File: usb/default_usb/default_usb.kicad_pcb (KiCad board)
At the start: 2 copper layers, 4 parts

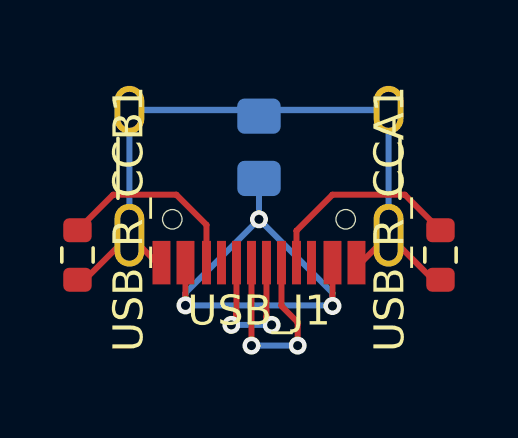
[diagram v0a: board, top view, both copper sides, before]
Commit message: updat e-paper module
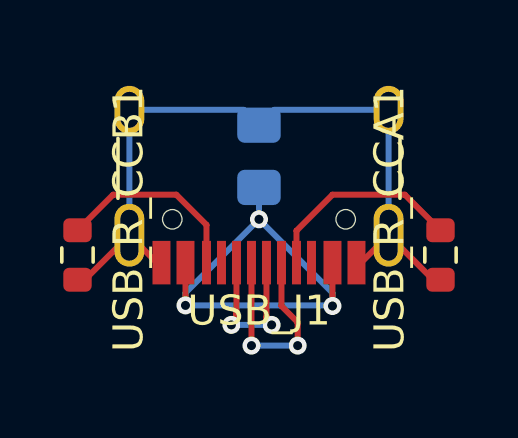
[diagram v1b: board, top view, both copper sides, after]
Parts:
- moved USB_C1 0.30 mm to (0.00, 0.50)
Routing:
- net GND: track 33.9 -> 25.5 mm
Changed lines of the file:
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@@
 		(fp_line
 			(start 5.32 -5.27)
-			(end 5.32 2.6)
-			(stroke
-				(width 0.05)
-				(type solid)
-			)
-			(layer "F.CrtYd")
-		)
-		(fp_line
-			(start -5.32 2.6)
-			(end 5.32 2.6)
+			(end 5.32 2.4)
+			(stroke
+				(width 0.05)
+				(type solid)
+			)
+			(layer "F.CrtYd")
+		)
+		(fp_line
+			(start -5.32 2.4)
+			(end 5.32 2.4)
 			(stroke
 				(width 0.05)
@@
 		(fp_line
 			(start -5.32 -5.27)
-			(end -5.32 2.6)
+			(end -5.32 2.4)
 			(stroke
 				(width 0.05)
@@
 		)
 		(embedded_fonts no)
-		(model "/Users/jinsongc/Development/ErgoCaiLib/3dmodels/TYPE-C-31-M-12--3DModel-STEP-56544.STEP"
+		(model "${KICAD8_3RD_PARTY}/3dmodels/com_github_ebastler_marbastlib/CON_TYPE-C-31-M-12.step"
 			(offset
-				(xyz 0 -1 0.04)
+				(xyz -4.47 -3.65 0.04)
 			)
 			(scale
@@
 			)
 			(rotate
-				(xyz 90 180 -180)
+				(xyz 0 0 0)
 			)
 		)
@@
 	(footprint "ErgoCai.pretty:C_0805_2012Metric_Pad1.18x1.45mm_HandSolder"
 		(layer "B.Cu")
-		(at 0 0.2 -90)
+		(at 0 0.5 -90)
 		(descr "Capacitor SMD 0805 (2012 Metric), square (rectangular) end terminal, IPC_7351 nominal with elongated pad for handsoldering. (Body size source: IPC-SM-782 page 76, https://www.pcb-3d.com/wordpress/wp-content/uploads/ipc-sm-782a_amendment_1_and_2.pdf, https://docs.google.com/spreadsheets/d/1BsfQQcO9C6DZCsRaXUlFlo91Tg2WpOkGARC1WS5S8t0/edit?usp=sharing), generated with kicad-footprint-generator")
 		(tags "capacitor handsolder")
@@
 	)
 	(segment
-		(start 0 1.2375)
-		(end 0 2.6)
+		(start 2.43 5.47)
+		(end 2.45 5.49)
+		(width 0.2)
+		(layer "B.Cu")
+		(net 1)
+	)
+	(segment
+		(start 0 2.6)
+		(end -2.45 5.05)
 		(width 0.2)
 		(layer "B.Cu")
@@
 	(segment
 		(start -2.45 5.47)
-		(end -2.45 5.05)
+		(end 2.43 5.47)
 		(width 0.2)
 		(layer "B.Cu")
@@
 	)
 	(segment
-		(start 2.43 5.47)
-		(end 2.45 5.49)
+		(start 0 2.6)
+		(end 0 1.5375)
+		(width 0.2)
+		(layer "B.Cu")
+		(net 1)
+	)
+	(segment
+		(start 0 2.6)
+		(end 2.45 5.05)
 		(width 0.2)
 		(layer "B.Cu")
@@
 	(segment
 		(start -2.45 5.05)
-		(end 0 2.6)
-		(width 0.2)
-		(layer "B.Cu")
-		(net 1)
-	)
-	(segment
-		(start -2.45 5.47)
-		(end 2.43 5.47)
+		(end -2.45 5.47)
 		(width 0.2)
 		(layer "B.Cu")
@@
 	)
 	(segment
-		(start 0 2.6)
-		(end 2.45 5.05)
-		(width 0.2)
-		(layer "B.Cu")
-		(net 1)
-	)
-	(segment
 		(start -6.05 4.615)
 		(end -5.805 4.615)
@@
 	)
 	(segment
-		(start 0.2125 -1.05)
-		(end 0 -0.8375)
-		(width 0.2)
-		(layer "B.Cu")
-		(net 2)
-	)
-	(segment
 		(start 4.3075 -1.0375)
 		(end 4.32 -1.05)
@@
 	)
 	(segment
+		(start -4.32 -1.05)
+		(end -0.5125 -1.05)
+		(width 0.2)
+		(layer "B.Cu")
+		(net 2)
+	)
+	(segment
 		(start 4.32 -1.05)
 		(end 4.32 3.13)
@@
 	)
 	(segment
-		(start 0 -1.0375)
-		(end -4.3075 -1.0375)
-		(width 0.2)
-		(layer "B.Cu")
-		(net 2)
-	)
-	(segment
-		(start 0 -1.0375)
-		(end 4.3075 -1.0375)
-		(width 0.2)
-		(layer "B.Cu")
-		(net 2)
-	)
-	(segment
-		(start -0.2125 -1.05)
-		(end 0 -0.8375)
+		(start -0.5125 -1.05)
+		(end 0 -0.5375)
+		(width 0.2)
+		(layer "B.Cu")
+		(net 2)
+	)
+	(segment
+		(start 0.5125 -1.05)
+		(end 0 -0.5375)
+		(width 0.2)
+		(layer "B.Cu")
+		(net 2)
+	)
+	(segment
+		(start 4.32 -1.05)
+		(end 0.5125 -1.05)
 		(width 0.2)
 		(layer "B.Cu")
@@
 		(width 0.2)
 		(layer "B.Cu")
-		(net 2)
-	)
-	(segment
-		(start -4.32 -1.05)
-		(end -0.2125 -1.05)
-		(width 0.2)
-		(layer "B.Cu")
-		(net 2)
-	)
-	(segment
-		(start 4.32 -1.05)
-		(end 0.2125 -1.05)
-		(width 0.2)
-		(layer "B.Cu")

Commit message: update usb layout
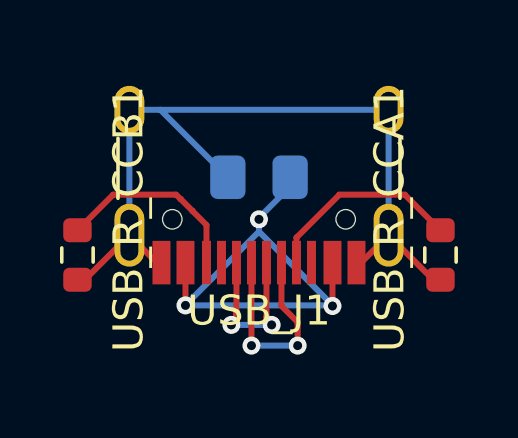
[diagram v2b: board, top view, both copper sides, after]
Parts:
- moved USB_C1 0.70 mm to (0.00, 1.20), turned to 0 degrees
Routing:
- net GND: track 25.5 -> 28.2 mm
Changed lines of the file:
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@@
 	(footprint "ErgoCai.pretty:C_0805_2012Metric_Pad1.18x1.45mm_HandSolder"
 		(layer "B.Cu")
-		(at 0 0.5 -90)
+		(at 0 1.2)
 		(descr "Capacitor SMD 0805 (2012 Metric), square (rectangular) end terminal, IPC_7351 nominal with elongated pad for handsoldering. (Body size source: IPC-SM-782 page 76, https://www.pcb-3d.com/wordpress/wp-content/uploads/ipc-sm-782a_amendment_1_and_2.pdf, https://docs.google.com/spreadsheets/d/1BsfQQcO9C6DZCsRaXUlFlo91Tg2WpOkGARC1WS5S8t0/edit?usp=sharing), generated with kicad-footprint-generator")
 		(tags "capacitor handsolder")
 		(property "Reference" "USB_C1"
-			(at -2.61 0 0)
+			(at -2.61 0 90)
 			(layer "B.SilkS")
 			(effects
@@
 		)
 		(property "Value" "10nF"
-			(at 2.29 0.03 0)
+			(at 2.29 0.03 90)
 			(layer "B.Fab")
 			(effects
@@
 		)
 		(property "Datasheet" ""
-			(at 0 0 90)
+			(at 0 0 180)
 			(unlocked yes)
 			(layer "B.Fab")
@@
 		)
 		(property "Description" ""
-			(at 0 0 90)
+			(at 0 0 180)
 			(unlocked yes)
 			(layer "B.Fab")
@@
 		(attr smd)
 		(fp_line
+			(start -0.261252 -0.735)
+			(end 0.261252 -0.735)
+			(stroke
+				(width 0.12)
+				(type solid)
+			)
+			(layer "B.SilkS")
+		)
+		(fp_line
 			(start -0.261252 0.735)
 			(end 0.261252 0.735)
@@
 		)
 		(fp_line
-			(start -0.261252 -0.735)
-			(end 0.261252 -0.735)
-			(stroke
-				(width 0.12)
-				(type solid)
-			)
-			(layer "B.SilkS")
+			(start -1.88 -0.98)
+			(end -1.88 0.98)
+			(stroke
+				(width 0.05)
+				(type solid)
+			)
+			(layer "B.CrtYd")
 		)
 		(fp_line
@@
 		)
 		(fp_line
+			(start 1.88 -0.98)
+			(end -1.88 -0.98)
+			(stroke
+				(width 0.05)
+				(type solid)
+			)
+			(layer "B.CrtYd")
+		)
+		(fp_line
 			(start 1.88 0.98)
 			(end 1.88 -0.98)
@@
 		)
 		(fp_line
-			(start -1.88 -0.98)
-			(end -1.88 0.98)
-			(stroke
-				(width 0.05)
-				(type solid)
-			)
-			(layer "B.CrtYd")
-		)
-		(fp_line
-			(start 1.88 -0.98)
-			(end -1.88 -0.98)
-			(stroke
-				(width 0.05)
-				(type solid)
-			)
-			(layer "B.CrtYd")
+			(start -1 -0.625)
+			(end -1 0.625)
+			(stroke
+				(width 0.1)
+				(type solid)
+			)
+			(layer "B.Fab")
 		)
 		(fp_line
@@
 		)
 		(fp_line
+			(start 1 -0.625)
+			(end -1 -0.625)
+			(stroke
+				(width 0.1)
+				(type solid)
+			)
+			(layer "B.Fab")
+		)
+		(fp_line
 			(start 1 0.625)
 			(end 1 -0.625)
@@
 			(layer "B.Fab")
 		)
-		(fp_line
-			(start -1 -0.625)
-			(end -1 0.625)
-			(stroke
-				(width 0.1)
-				(type solid)
-			)
-			(layer "B.Fab")
-		)
-		(fp_line
-			(start 1 -0.625)
-			(end -1 -0.625)
-			(stroke
-				(width 0.1)
-				(type solid)
-			)
-			(layer "B.Fab")
-		)
 		(fp_text user "${REFERENCE}"
-			(at 0 0 90)
+			(at 0 0 0)
 			(layer "B.Fab")
 			(effects
@@
 		)
 		(pad "1" smd roundrect
-			(at -1.0375 0 270)
+			(at -1.0375 0)
 			(size 1.175 1.45)
 			(layers "B.Cu" "B.Mask" "B.Paste")
@@
 		)
 		(pad "2" smd roundrect
-			(at 1.0375 0 270)
+			(at 1.0375 0)
 			(size 1.175 1.45)
 			(layers "B.Cu" "B.Mask" "B.Paste")
@@
 	)
 	(segment
+		(start 1.0375 1.5125)
+		(end 0 2.55)
+		(width 0.2)
+		(layer "B.Cu")
+		(net 1)
+	)
+	(segment
 		(start 2.43 5.47)
 		(end 2.45 5.49)
@@
 	)
 	(segment
-		(start 0 2.6)
-		(end -2.45 5.05)
-		(width 0.2)
-		(layer "B.Cu")
-		(net 1)
-	)
-	(segment
 		(start -2.45 5.47)
 		(end 2.43 5.47)
@@
 	)
 	(segment
-		(start 2.45 5.05)
+		(start 2.45 5.46)
 		(end 2.45 5.49)
 		(width 0.2)
@@
 	)
 	(segment
+		(start -2.45 5.46)
+		(end -2.45 5.47)
+		(width 0.2)
+		(layer "B.Cu")
+		(net 1)
+	)
+	(segment
+		(start 0 3.01)
+		(end -2.45 5.46)
+		(width 0.2)
+		(layer "B.Cu")
+		(net 1)
+	)
+	(segment
+		(start 0 2.55)
+		(end 0 2.6)
+		(width 0.2)
+		(layer "B.Cu")
+		(net 1)
+	)
+	(segment
 		(start 0 2.6)
-		(end 0 1.5375)
-		(width 0.2)
-		(layer "B.Cu")
-		(net 1)
-	)
-	(segment
-		(start 0 2.6)
-		(end 2.45 5.05)
-		(width 0.2)
-		(layer "B.Cu")
-		(net 1)
-	)
-	(segment
-		(start -2.45 5.05)
-		(end -2.45 5.47)
+		(end 0 3.01)
+		(width 0.2)
+		(layer "B.Cu")
+		(net 1)
+	)
+	(segment
+		(start 0 3.01)
+		(end 2.45 5.46)
+		(width 0.2)
+		(layer "B.Cu")
+		(net 1)
+	)
+	(segment
+		(start 1.0375 1.2)
+		(end 1.0375 1.5125)
 		(width 0.2)
 		(layer "B.Cu")
@@
 	)
 	(segment
-		(start -4.32 -1.05)
-		(end -0.5125 -1.05)
+		(start -1.0375 1.2)
+		(end -3.2875 -1.05)
+		(width 0.2)
+		(layer "B.Cu")
+		(net 2)
+	)
+	(segment
+		(start -3.2875 -1.05)
+		(end 4.32 -1.05)
 		(width 0.2)
 		(layer "B.Cu")
@@
 	)
 	(segment
-		(start -0.5125 -1.05)
-		(end 0 -0.5375)
-		(width 0.2)
-		(layer "B.Cu")
-		(net 2)
-	)
-	(segment
-		(start 0.5125 -1.05)
-		(end 0 -0.5375)
-		(width 0.2)
-		(layer "B.Cu")
-		(net 2)
-	)
-	(segment
-		(start 4.32 -1.05)
-		(end 0.5125 -1.05)
+		(start -4.32 -1.05)
+		(end -3.2875 -1.05)
 		(width 0.2)
 		(layer "B.Cu")
@@
 	)
 	(segment
-		(start 1.25 2.98)
-		(end 1.25 4.045)
+		(start 6.046 2.965)
+		(end 4.86 1.779)
 		(width 0.2)
 		(layer "F.Cu")
@@
 	)
 	(segment
-		(start 4.86 1.779)
-		(end 2.451 1.779)
-		(width 0.2)
-		(layer "F.Cu")
-		(net 4)
-	)
-	(segment
-		(start 2.451 1.779)
-		(end 1.25 2.98)
+		(start 2.681 1.779)
+		(end 1.25 3.21)
 		(width 0.2)
 		(layer "F.Cu")
@@
 	)
 	(segment
-		(start 6.046 2.965)
-		(end 4.86 1.779)
+		(start 4.86 1.779)
+		(end 2.681 1.779)
+		(width 0.2)
+		(layer "F.Cu")
+		(net 4)
+	)
+	(segment
+		(start 1.25 3.21)
+		(end 1.25 4.045)
 		(width 0.2)
 		(layer "F.Cu")
@@
 	)
 	(segment
+		(start -4.86 1.779)
+		(end -2.761 1.779)
+		(width 0.2)
+		(layer "F.Cu")
+		(net 6)
+	)
+	(segment
+		(start -2.609992 1.924)
+		(end -2.214 2.319992)
+		(width 0.2)
+		(layer "F.Cu")
+		(net 6)
+	)
+	(segment
+		(start -2.616 1.924)
+		(end -2.609992 1.924)
+		(width 0.2)
+		(layer "F.Cu")
+		(net 6)
+	)
+	(segment
+		(start -2.214 2.326)
+		(end -1.75 2.79)
+		(width 0.2)
+		(layer "F.Cu")
+		(net 6)
+	)
+	(segment
+		(start -2.214 2.319992)
+		(end -2.214 2.326)
+		(width 0.2)
+		(layer "F.Cu")
+		(net 6)
+	)
+	(segment
 		(start -6.05 2.965)
 		(end -6.046 2.965)
@@
 	)
 	(segment
-		(start -2.754992 1.779)
-		(end -1.75 2.783992)
-		(width 0.2)
-		(layer "F.Cu")
-		(net 6)
-	)
-	(segment
-		(start -4.86 1.779)
-		(end -2.754992 1.779)
+		(start -2.761 1.779)
+		(end -2.616 1.924)
+		(width 0.2)
+		(layer "F.Cu")
+		(net 6)
+	)
+	(segment
+		(start -1.75 2.79)
+		(end -1.75 4.045)
 		(width 0.2)
 		(layer "F.Cu")
@@
 		(width 0.2)
 		(layer "F.Cu")
-		(net 6)
-	)
-	(segment
-		(start -1.75 2.783992)
-		(end -1.75 4.045)
-		(width 0.2)
-		(layer "F.Cu")

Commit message: update via pos in usb
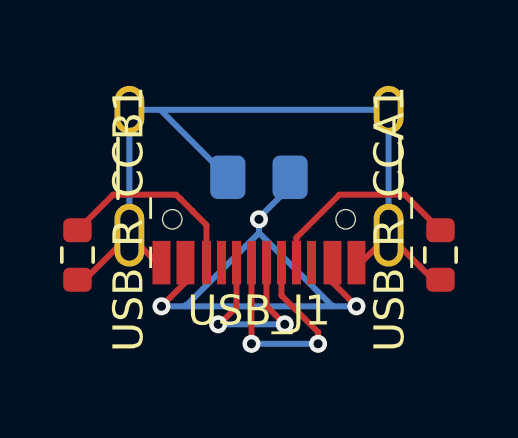
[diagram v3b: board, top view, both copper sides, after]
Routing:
- net VBUS: track 17.0 -> 19.4 mm
- net DATA-: track 7.30 -> 8.25 mm
- net DATA+: track 6.28 -> 7.02 mm
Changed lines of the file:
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@@
 	)
 	(segment
-		(start -2.45 4.045)
-		(end -2.45 5.47)
+		(start 2.45 4.7)
+		(end 3.25 5.5)
+		(width 0.2)
+		(layer "F.Cu")
+		(net 1)
+	)
+	(segment
+		(start -2.45 4.7)
+		(end -2.45 4.045)
+		(width 0.2)
+		(layer "F.Cu")
+		(net 1)
+	)
+	(segment
+		(start -3.25 5.5)
+		(end -2.45 4.7)
 		(width 0.2)
 		(layer "F.Cu")
@@
 	(segment
 		(start 2.45 4.045)
-		(end 2.45 5.49)
-		(width 0.2)
-		(layer "F.Cu")
-		(net 1)
-	)
-	(via
-		(at -2.45 5.47)
-		(size 0.6)
-		(drill 0.3)
-		(layers "F.Cu" "B.Cu")
-		(net 1)
-	)
-	(via
-		(at 2.45 5.49)
+		(end 2.45 4.7)
+		(width 0.2)
+		(layer "F.Cu")
+		(net 1)
+	)
+	(via
+		(at -3.25 5.5)
+		(size 0.6)
+		(drill 0.3)
+		(layers "F.Cu" "B.Cu")
+		(net 1)
+	)
+	(via
+		(at 3.25 5.5)
 		(size 0.6)
 		(drill 0.3)
@@
 	)
 	(segment
-		(start -2.45 5.47)
-		(end 2.43 5.47)
-		(width 0.2)
-		(layer "B.Cu")
-		(net 1)
-	)
-	(segment
-		(start 2.45 5.46)
-		(end 2.45 5.49)
+		(start -3.27 5.5)
+		(end 3.25 5.5)
 		(width 0.2)
 		(layer "B.Cu")
@@
 	)
 	(segment
-		(start 0 3.01)
-		(end -2.45 5.46)
-		(width 0.2)
-		(layer "B.Cu")
-		(net 1)
-	)
-	(segment
 		(start 0 2.55)
 		(end 0 2.6)
@@
 	)
 	(segment
-		(start 0 2.6)
-		(end 0 3.01)
-		(width 0.2)
-		(layer "B.Cu")
-		(net 1)
-	)
-	(segment
-		(start 0 3.01)
-		(end 2.45 5.46)
+		(start 2.45 5.5)
+		(end 0 3.05)
 		(width 0.2)
 		(layer "B.Cu")
@@
 	)
 	(segment
+		(start 0 3.05)
+		(end -2.45 5.5)
+		(width 0.2)
+		(layer "B.Cu")
+		(net 1)
+	)
+	(segment
+		(start 0 2.6)
+		(end 0 3.05)
+		(width 0.2)
+		(layer "B.Cu")
+		(net 1)
+	)
+	(segment
 		(start 0 2.59)
 		(end -0.01 2.6)
@@
 	)
 	(segment
-		(start 1.29 6.05)
-		(end 1.29 6.81)
-		(width 0.2)
-		(layer "F.Cu")
-		(net 3)
-	)
-	(segment
-		(start 1.3 6.04)
-		(end 1.29 6.05)
-		(width 0.2)
-		(layer "F.Cu")
-		(net 3)
-	)
-	(segment
-		(start 0.75 5.49)
-		(end 1.3 6.04)
-		(width 0.2)
-		(layer "F.Cu")
-		(net 3)
-	)
-	(segment
 		(start 0.75 4.045)
-		(end 0.75 5.49)
+		(end 0.75 5.14)
+		(width 0.2)
+		(layer "F.Cu")
+		(net 3)
+	)
+	(segment
+		(start 1.97 6.36)
+		(end 0.75 5.14)
+		(width 0.2)
+		(layer "F.Cu")
+		(net 3)
+	)
+	(segment
+		(start 1.97 6.75)
+		(end 1.97 6.36)
 		(width 0.2)
 		(layer "F.Cu")
@@
 	)
 	(via
-		(at 1.29 6.81)
-		(size 0.6)
-		(drill 0.3)
-		(layers "F.Cu" "B.Cu")
-		(net 3)
-	)
-	(via
-		(at -0.25 6.81)
-		(size 0.6)
-		(drill 0.3)
-		(layers "F.Cu" "B.Cu")
-		(net 3)
-	)
-	(segment
-		(start -0.25 6.81)
-		(end 1.29 6.81)
+		(at 1.97 6.75)
+		(size 0.6)
+		(drill 0.3)
+		(layers "F.Cu" "B.Cu")
+		(net 3)
+	)
+	(via
+		(at -0.25 6.75)
+		(size 0.6)
+		(drill 0.3)
+		(layers "F.Cu" "B.Cu")
+		(net 3)
+	)
+	(segment
+		(start -0.25 6.75)
+		(end 1.97 6.75)
+		(width 0.2)
+		(layer "B.Cu")
+		(net 3)
+	)
+	(segment
+		(start -0.25 6.71)
+		(end -0.21 6.75)
 		(width 0.2)
 		(layer "B.Cu")
@@
 	)
 	(segment
-		(start 0.25 5.852959)
-		(end 0.25 5.947946)
-		(width 0.2)
-		(layer "F.Cu")
-		(net 5)
-	)
-	(segment
-		(start 0.25 5.852959)
-		(end 0.422054 6.025013)
-		(width 0.2)
-		(layer "F.Cu")
-		(net 5)
-	)
-	(segment
-		(start -0.75 5.91)
-		(end -0.92 6.08)
-		(width 0.2)
-		(layer "F.Cu")
-		(net 5)
-	)
-	(segment
-		(start -0.75 5.95)
-		(end -0.92 6.12)
+		(start -0.75 5.53)
+		(end -1.36 6.14)
+		(width 0.2)
+		(layer "F.Cu")
+		(net 5)
+	)
+	(segment
+		(start 0.25 5.49)
+		(end 0.86 6.1)
+		(width 0.2)
+		(layer "F.Cu")
+		(net 5)
+	)
+	(segment
+		(start 0.25 4.045)
+		(end 0.25 5.49)
 		(width 0.2)
 		(layer "F.Cu")
@@
 	(segment
 		(start -0.75 4.045)
-		(end -0.75 5.75)
-		(width 0.2)
-		(layer "F.Cu")
-		(net 5)
-	)
-	(segment
-		(start 0.25 5.947946)
-		(end 0.422054 6.12)
-		(width 0.2)
-		(layer "F.Cu")
-		(net 5)
-	)
-	(segment
-		(start -0.75 5.75)
-		(end -0.75 5.95)
-		(width 0.2)
-		(layer "F.Cu")
-		(net 5)
-	)
-	(segment
-		(start -0.75 5.75)
-		(end -0.75 5.91)
-		(width 0.2)
-		(layer "F.Cu")
-		(net 5)
-	)
-	(segment
-		(start 0.25 4.045)
-		(end 0.25 5.852959)
-		(width 0.2)
-		(layer "F.Cu")
-		(net 5)
-	)
-	(via
-		(at -0.92 6.12)
-		(size 0.6)
-		(drill 0.3)
-		(layers "F.Cu" "B.Cu")
-		(net 5)
-	)
-	(via
-		(at 0.422054 6.12)
-		(size 0.6)
-		(drill 0.3)
-		(layers "F.Cu" "B.Cu")
-		(net 5)
-	)
-	(segment
-		(start -0.92 6.12)
-		(end 0.422054 6.12)
-		(width 0.2)
-		(layer "B.Cu")
+		(end -0.75 5.53)
+		(width 0.2)
+		(layer "F.Cu")
+		(net 5)
+	)
+	(via
+		(at -1.36 6.1)
+		(size 0.6)
+		(drill 0.3)
+		(layers "F.Cu" "B.Cu")
+		(net 5)
+	)
+	(via
+		(at 0.86 6.1)
+		(size 0.6)
+		(drill 0.3)
+		(layers "F.Cu" "B.Cu")
+		(net 5)
+	)
+	(segment
+		(start -1.36 6.14)
+		(end -1.32 6.1)
+		(width 0.2)
+		(layer "B.Cu")
+		(net 5)
+	)
+	(segment
+		(start 0.71 6.1)
+		(end 0.74 6.13)
+		(width 0.2)
+		(layer "B.Cu")
+		(net 5)
+	)
+	(segment
+		(start -1.36 6.1)
+		(end 0.86 6.1)
+		(width 0.2)
+		(layer "B.Cu")
+		(net 5)
+	)
+	(segment
+		(start -1.27 6.09)
+		(end -1.24 6.12)
+		(width 0.2)
+		(layer "B.Cu")
